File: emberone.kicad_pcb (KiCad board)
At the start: 6 copper layers, 125 x 125 mm, 409 parts, among them J1 Screw Terminal, J10 Conn_01x01, J11 Conn_01x01, J14 Conn_01x01, J15 Conn_01x01, J18 Conn_01x01, J19 Conn_Coaxial, J2 Screw Terminal, J20 Conn_01x06, J21 Conn_01x01, J3 Conn_01x01, J4 Conn_01x01, J5 Conn_01x01, J6 USB_C_Receptacle_USB2.0, J7 Conn_01x01, J8 Conn_01x01, J9 Conn_01x01, Q1 CSD18511Q5A, Q2 CSD18511Q5A, Q3 CSD18511Q5A, Q4 CSD18511Q5A, Q5 NVMFS5C645NLAFT1G, SW1 GT-TC029B-H025-L1N, SW2 GT-TC029B-H025-L1N, U1 LM25119PSQ/NOPB, U10 TLV1117LV33DCYR, U11 TPD1E05U06DYA, U12 TPD1E05U06DYA, U13 TMP451HQDQWRQ1, U2 DS4432U+, U27 RP2040, U28 MCP1824T-1202E/OT, U29 MCP1824T-1202E/OT, U3 INA260, U30 MCP1824T-1202E/OT, U32 MCP1824T-0802E, U4 SN74AVC4T774, U42 MCP1824T-0802E, U43 MCP1824T-0802E, U45 BM1362AC_MODE1, U46 BM1362AC_MODE0, U47 BM1362AC_MODE1, U48 MCP1824T-1202E/OT, U49 MCP1824T-1202E/OT, U5 25MHz, U50 MCP1824T-1202E/OT, U51 MCP1824T-0802E, U52 MCP1824T-0802E, U53 MCP1824T-0802E, U54 BM1362AC_MODE1, U55 BM1362AC_MODE0, U56 BM1362AC_MODE1, U57 MCP1824T-1202E/OT, U58 MCP1824T-1202E/OT, U59 MCP1824T-1202E/OT, U6 TMP1075, U60 MCP1824T-0802E, U61 MCP1824T-0802E, U62 MCP1824T-0802E, U63 BM1362AC_MODE1, U64 BM1362AC_MODE0, U65 BM1362AC_MODE1, U66 MCP1824T-1202E/OT, U67 MCP1824T-1202E/OT, U68 MCP1824T-1202E/OT, U69 MCP1824T-0802E, U7 AP74700Q, U70 MCP1824T-0802E, U71 MCP1824T-0802E, U72 BM1362AC_MODE1, U73 BM1362AC_MODE0, U74 BM1362AC_MODE1, U8 W25Q16JVUXIQ TR, U9 SK6812, Y1 12MHz

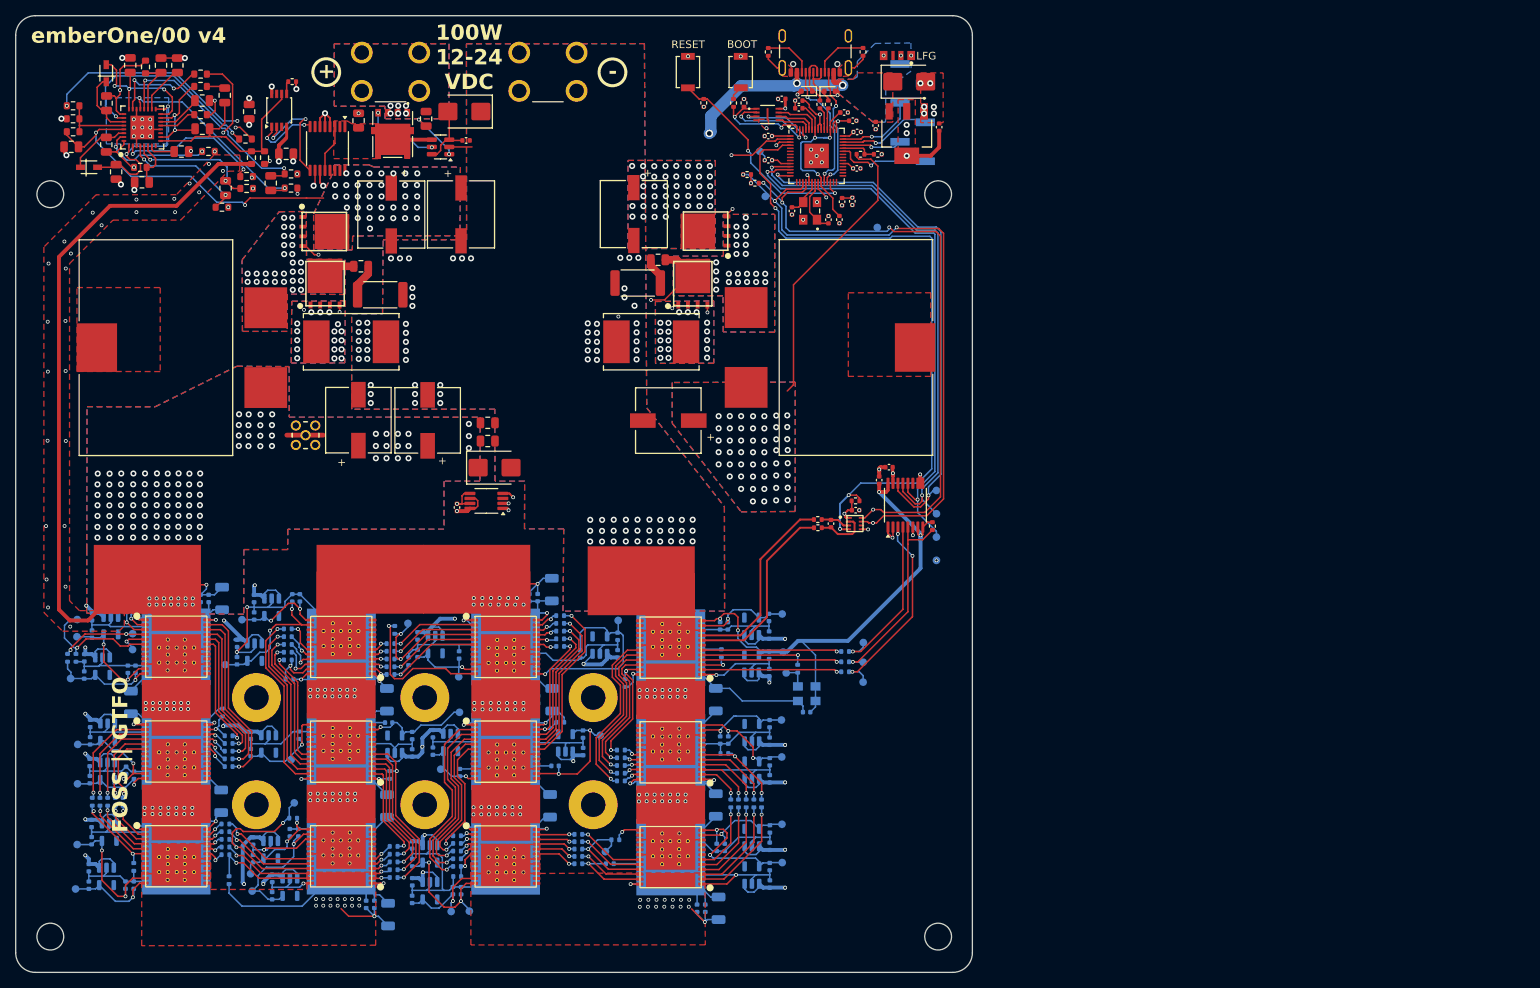
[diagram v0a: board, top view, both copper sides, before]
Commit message: fixup fiducials for #49
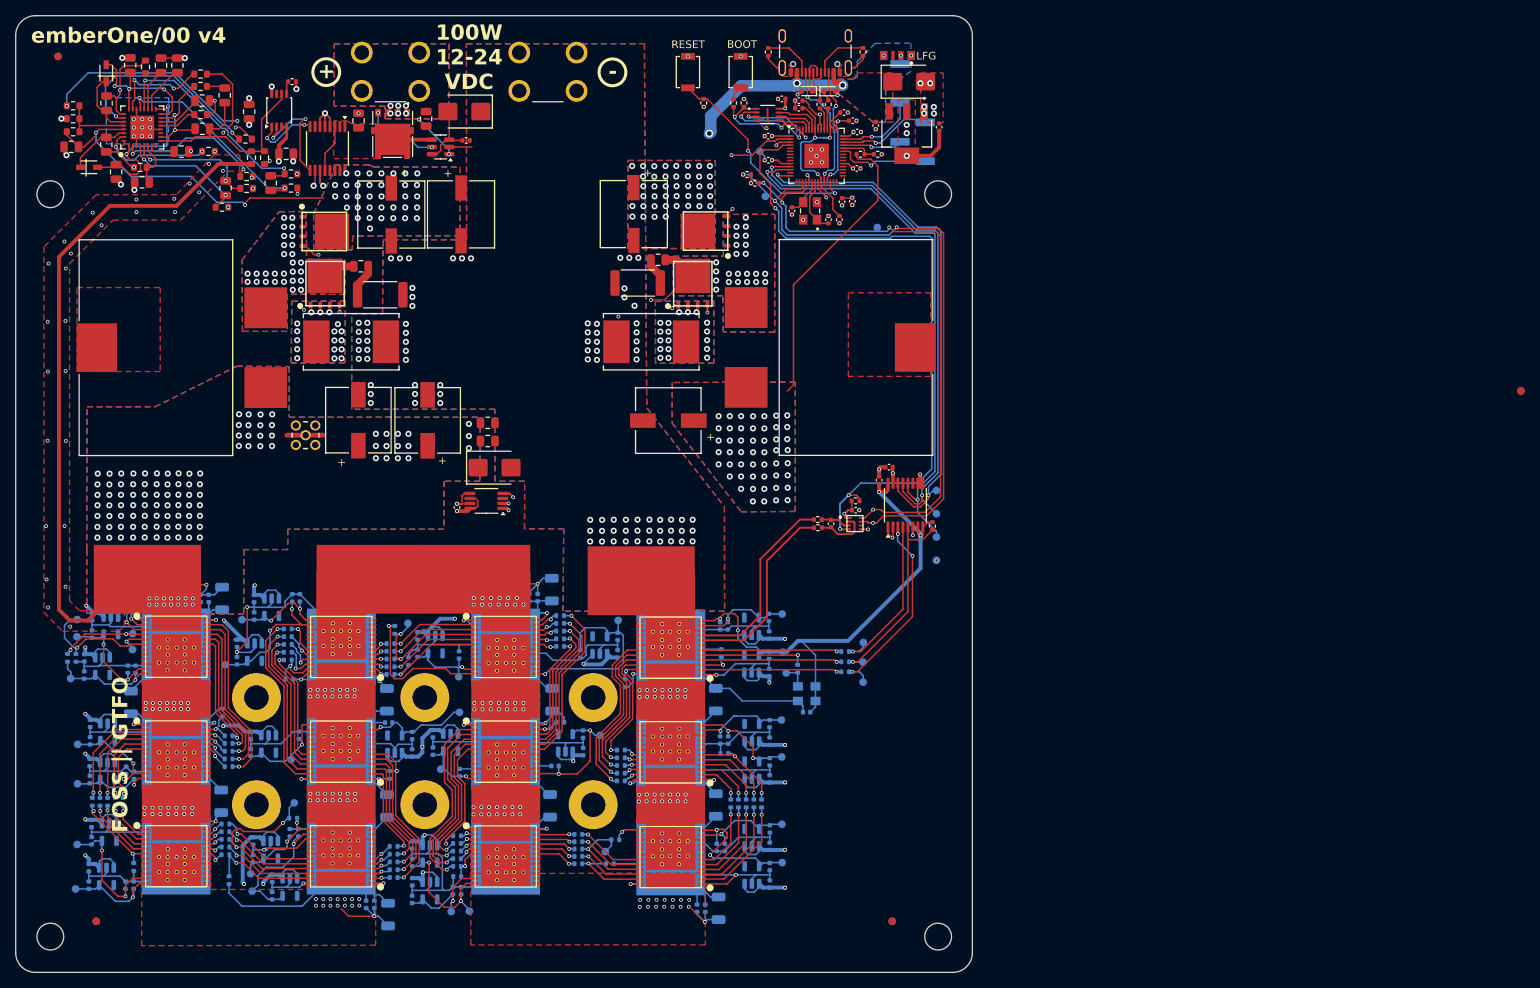
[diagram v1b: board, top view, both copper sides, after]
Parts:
- added FID1: Fiducial, emberone:Fiducial_1mm_Mask2mm, F.Cu at (123.0, 84.0)
- added FID2: Fiducial, emberone:Fiducial_1mm_Mask2mm, F.Cu at (128.0, 197.0)
- added FID3: Fiducial, emberone:Fiducial_1mm_Mask2mm, F.Cu at (232.0, 197.0)
- added FID4: Fiducial, emberone:Fiducial_1mm_Mask2mm, F.Cu at (314.1, 127.7)
